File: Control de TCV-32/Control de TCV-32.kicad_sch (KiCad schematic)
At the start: 6 parts, among them J1 Bocina, J2 Microfono, J3 Screw_Terminal_01x02, J5 HC-05, U1 LM7805_TO220

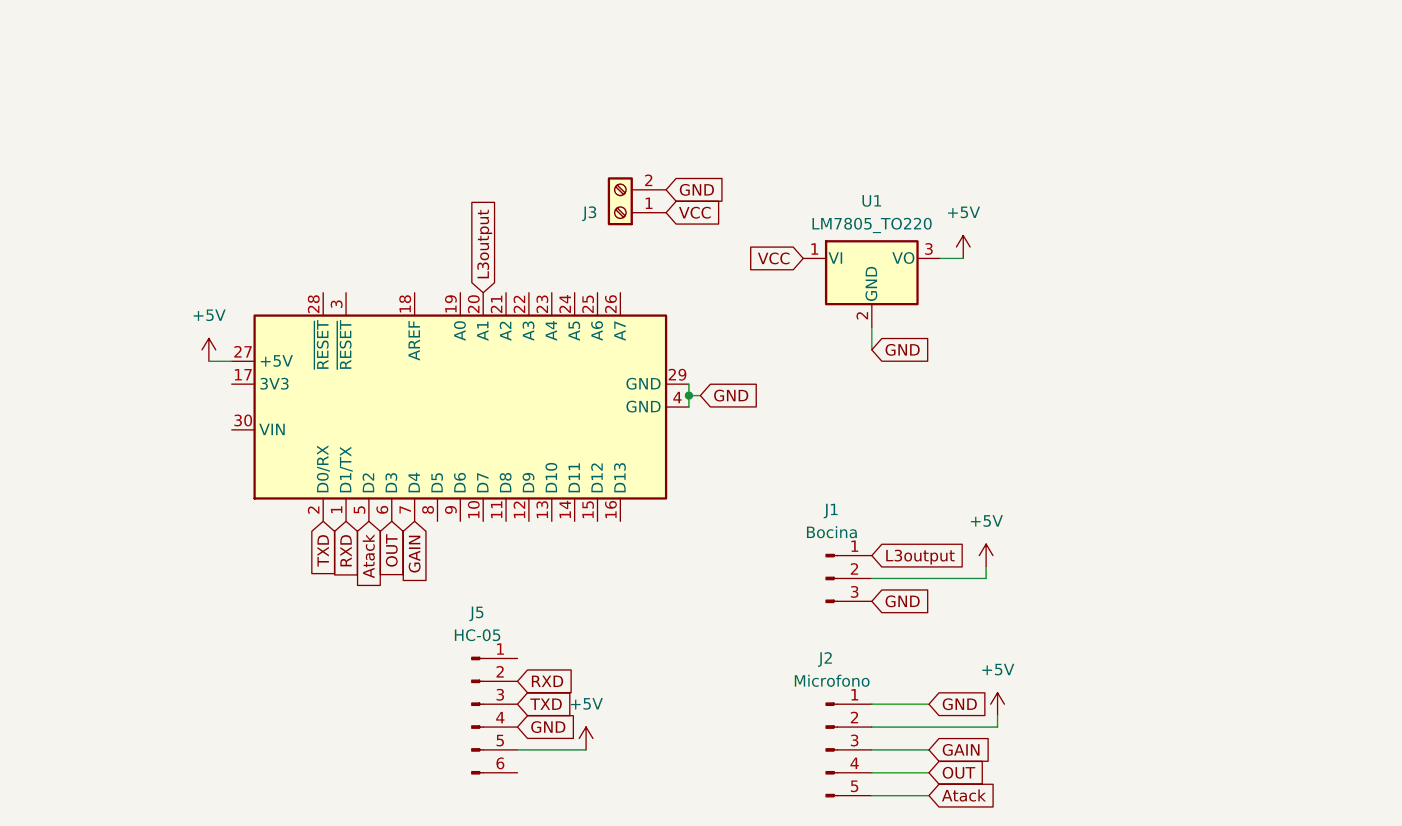
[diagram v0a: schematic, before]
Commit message: Cambio de componentes
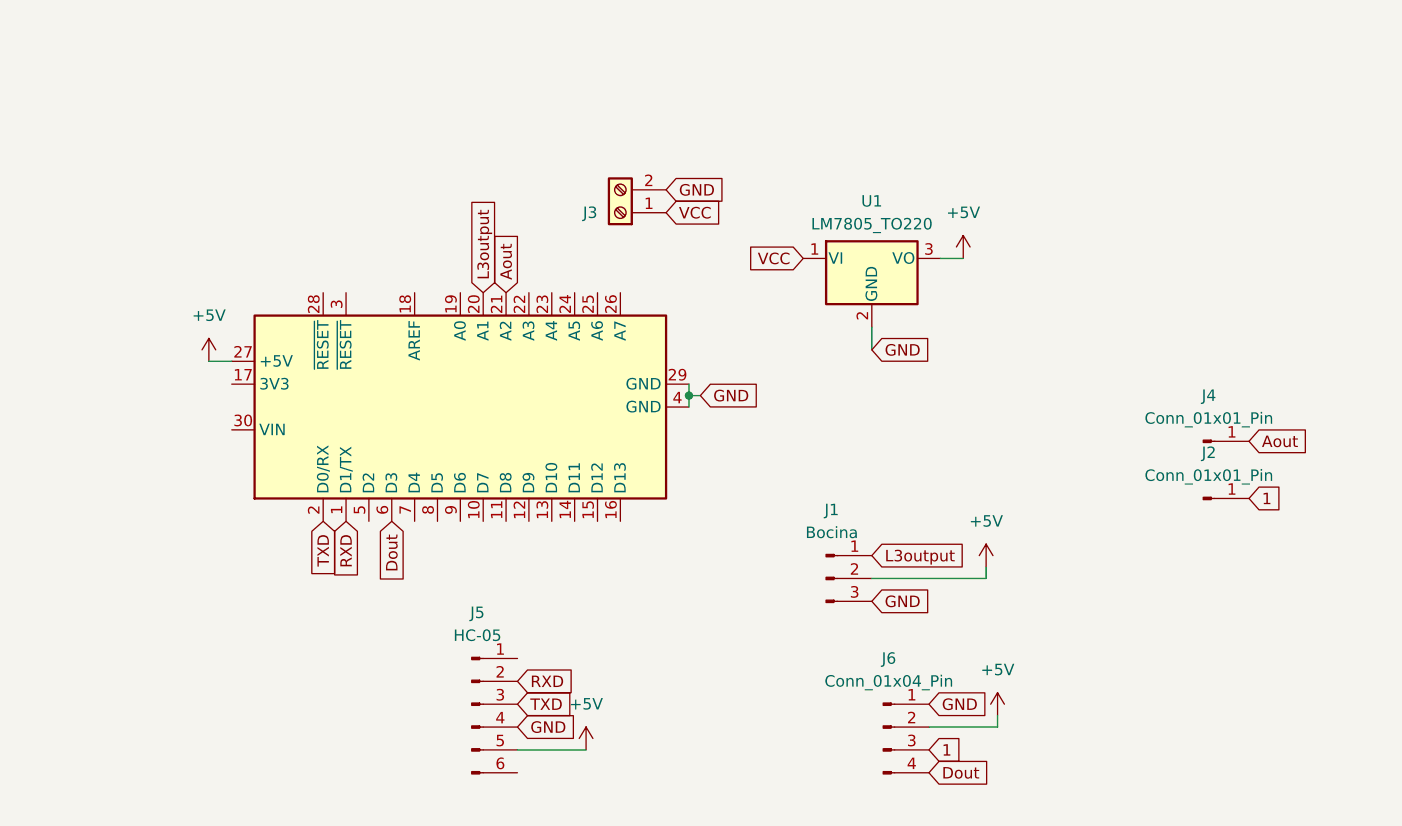
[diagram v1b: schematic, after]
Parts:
- removed J2: Microfono, Connector_PinHeader_2.54mm:PinHeader_1x05_P2.54mm_Vertical, symbol Connector:Conn_01x05_Pin
- added J2, J4: Conn_01x01_Pin, Connector_PinHeader_2.54mm:PinHeader_1x01_P2.54mm_Vertical, symbol Connector:Conn_01x01_Pin
- added J6: Conn_01x04_Pin, Connector_PinHeader_2.54mm:PinHeader_1x04_P2.54mm_Vertical, symbol Connector:Conn_01x04_Pin
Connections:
- net +5V: now also J6.2 (Pin_2)
- net GND: now also J6.1 (Pin_1)
- net Aout: now reaches A2.21 (A2)
- net Aout: now also J4.1 (Pin_1)
- net Atack: no longer names the net of A2.5 (D2)
- net GAIN: no longer names the net of A2.7 (D4)
- net OUT renamed Dout
- net Dout: now also J6.4 (Pin_4)
- new net 1: J2.1 (Pin_1), J6.3 (Pin_3)

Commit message: Placa C modificada con ESP32 C3
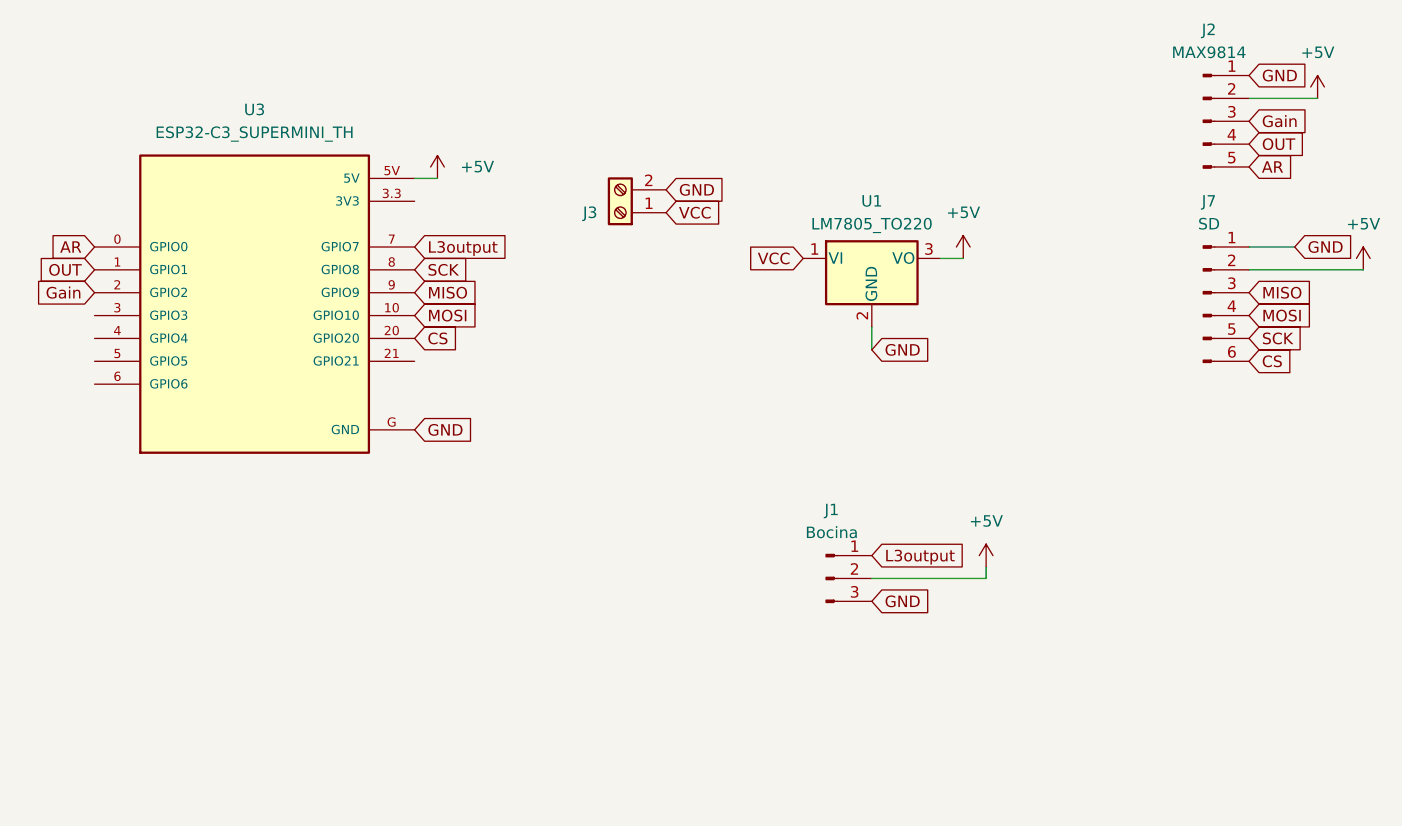
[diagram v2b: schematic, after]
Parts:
- removed A2: Arduino_Nano_v3.x, Module:Arduino_Nano, symbol MCU_Module:Arduino_Nano_v3.x
- removed J2, J4: Conn_01x01_Pin, Connector_PinHeader_2.54mm:PinHeader_1x01_P2.54mm_Vertical, symbol Connector:Conn_01x01_Pin
- removed J5: HC-05, Connector_PinHeader_2.54mm:PinHeader_1x06_P2.54mm_Vertical, symbol Connector:Conn_01x06_Pin
- removed J6: Conn_01x04_Pin, Connector_PinHeader_2.54mm:PinHeader_1x04_P2.54mm_Vertical, symbol Connector:Conn_01x04_Pin
- added J2: MAX9814, Connector_PinHeader_2.54mm:PinHeader_1x05_P2.54mm_Vertical, symbol Connector:Conn_01x05_Pin
- added J7: SD, Connector_PinHeader_2.54mm:PinHeader_1x06_P2.54mm_Vertical, symbol Connector:Conn_01x06_Pin
- added U3: ESP32-C3_SUPERMINI_TH, huellas:MODULE_ESP32-C3_SUPERMINI_TH, symbol ESP32-C3_SUPERMINI_TH:ESP32-C3_SUPERMINI_TH
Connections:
- net +5V: now also J2.2 (Pin_2), J7.2 (Pin_2), U3.5V
- net GND: now also J2.1 (Pin_1), J7.1 (Pin_1), U3.G (GND)
- net L3output: now also U3.7 (GPIO7)
- new net AR: J2.5 (Pin_5), U3.0 (GPIO0)
- new net CS: J7.6 (Pin_6), U3.20 (GPIO20)
- new net Gain: J2.3 (Pin_3), U3.2 (GPIO2)
- new net MISO: J7.3 (Pin_3), U3.9 (GPIO9)
- new net MOSI: J7.4 (Pin_4), U3.10 (GPIO10)
- new net OUT: J2.4 (Pin_4), U3.1 (GPIO1)
- new net SCK: J7.5 (Pin_5), U3.8 (GPIO8)
